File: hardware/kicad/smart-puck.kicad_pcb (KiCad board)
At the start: 2 copper layers, 3 parts, among them U1 ESP32-C6-MINI-1, U2 TPS63900, U3 SHT4x

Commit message: worked on schematic
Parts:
- added J1: HLK-LD2420, Connector_PinHeader_2.54mm:PinHeader_1x04_P2.54mm_Vertical, F.Cu at (125.8, 112.3)
- added U4: BQ25185DLHR, BQ25185:WSON10_DLH_TEX, F.Cu at (136.5, 113.0)
- added U5: MAX17048G+T10, MAX17048G:21-0168E_T822-3_MXM, F.Cu at (136.0, 118.2)

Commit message: worked on schematic
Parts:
- added J2: HLK-LD2420, Connector_PinSocket_2.54mm:PinSocket_1x05_P2.54mm_Vertical, F.Cu at (146.8, 141.8)
- added U2: TPS63900, Package_SON:WSON-10-1EP_2.5x2.5mm_P0.5mm_EP1.2x2mm_ThermalVias, F.Cu at (151.9, 141.5)
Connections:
- U1 pad 1: Net-(U1-GND-Pad1) -> BAT-
- U1 pad 11: Net-(U1-GND-Pad1) -> BAT-
- U1 pad 12: unconnected-(U1-IO0-Pad12) -> OT2
- U1 pad 14: Net-(U1-GND-Pad1) -> BAT-
- U1 pad 17: unconnected-(U1-IO12-Pad17) -> D-
- U1 pad 18: unconnected-(U1-IO13-Pad18) -> D+
- U1 pad 2: Net-(U1-GND-Pad1) -> BAT-
- U1 pad 22: unconnected-(U1-IO8-Pad22) -> BOOT
- U1 pad 24: unconnected-(U1-IO18-Pad24) -> RX
- U1 pad 25: unconnected-(U1-IO19-Pad25) -> TX
- U1 pad 27: unconnected-(U1-IO21-Pad27) -> LED_R
- U1 pad 28: unconnected-(U1-IO22-Pad28) -> LED_G
- U1 pad 29: unconnected-(U1-IO23-Pad29) -> LED_B
- U1 pad 3: unconnected-(U1-3V3-Pad3) -> +3.3V
- U1 pad 36: Net-(U1-GND-Pad1) -> BAT-
- U1 pad 37: Net-(U1-GND-Pad1) -> BAT-
- U1 pad 38: Net-(U1-GND-Pad1) -> BAT-
- U1 pad 39: Net-(U1-GND-Pad1) -> BAT-
- U1 pad 40: Net-(U1-GND-Pad1) -> BAT-
- U1 pad 41: Net-(U1-GND-Pad1) -> BAT-
- U1 pad 42: Net-(U1-GND-Pad1) -> BAT-
- U1 pad 43: Net-(U1-GND-Pad1) -> BAT-
- U1 pad 44: Net-(U1-GND-Pad1) -> BAT-
- U1 pad 45: Net-(U1-GND-Pad1) -> BAT-
- U1 pad 46: Net-(U1-GND-Pad1) -> BAT-
- U1 pad 47: Net-(U1-GND-Pad1) -> BAT-
- U1 pad 48: Net-(U1-GND-Pad1) -> BAT-
- U1 pad 49: Net-(U1-GND-Pad1) -> BAT-
- U1 pad 5: unconnected-(U1-IO2-Pad5) -> SDA
- U1 pad 50: Net-(U1-GND-Pad1) -> BAT-
- U1 pad 51: Net-(U1-GND-Pad1) -> BAT-
- U1 pad 52: Net-(U1-GND-Pad1) -> BAT-
- U1 pad 53: Net-(U1-GND-Pad1) -> BAT-
- U1 pad 6: unconnected-(U1-IO3-Pad6) -> SCL
- U1 pad 8: unconnected-(U1-EN-Pad8) -> EN
- U3 pad 1: unconnected-(U3-SDA-Pad1) -> SDA
- U3 pad 2: unconnected-(U3-SCL-Pad2) -> SCL
- U3 pad 3: unconnected-(U3-VDD-Pad3) -> +3.3V
- U3 pad 4: unconnected-(U3-VSS-Pad4) -> BAT-
- U4 pad 1: unconnected-(U4-SYS-Pad1) -> Net-(U4-SYS)
- U4 pad 10: unconnected-(U4-IN-Pad10) -> +5V
- U4 pad 11: unconnected-(U4-EPAD-Pad11) -> BAT-
- U4 pad 2: unconnected-(U4-BAT-Pad2) -> BAT+
- U4 pad 4: unconnected-(U4-/CE-Pad4) -> BAT-
- U4 pad 5: unconnected-(U4-GND-Pad5) -> BAT-
- U4 pad 6: unconnected-(U4-TS/MR-Pad6) -> Net-(U4-TS/MR)
- U4 pad 7: unconnected-(U4-ILIM/VSET-Pad7) -> Net-(U4-ILIM/VSET)
- U4 pad 8: unconnected-(U4-ISET-Pad8) -> Net-(U4-ISET)
- U5 pad 1: unconnected-(U5-CTG-Pad1) -> BAT-
- U5 pad 3: unconnected-(U5-VDD-Pad3) -> BAT+
- U5 pad 4: unconnected-(U5-GND-Pad4) -> BAT-
- U5 pad 6: unconnected-(U5-QSTRT-Pad6) -> BAT-
- U5 pad 7: unconnected-(U5-SCL-Pad7) -> SCL
- U5 pad 8: unconnected-(U5-SDA-Pad8) -> SDA
- U5 pad 9: unconnected-(U5-EPAD-Pad9) -> BAT-

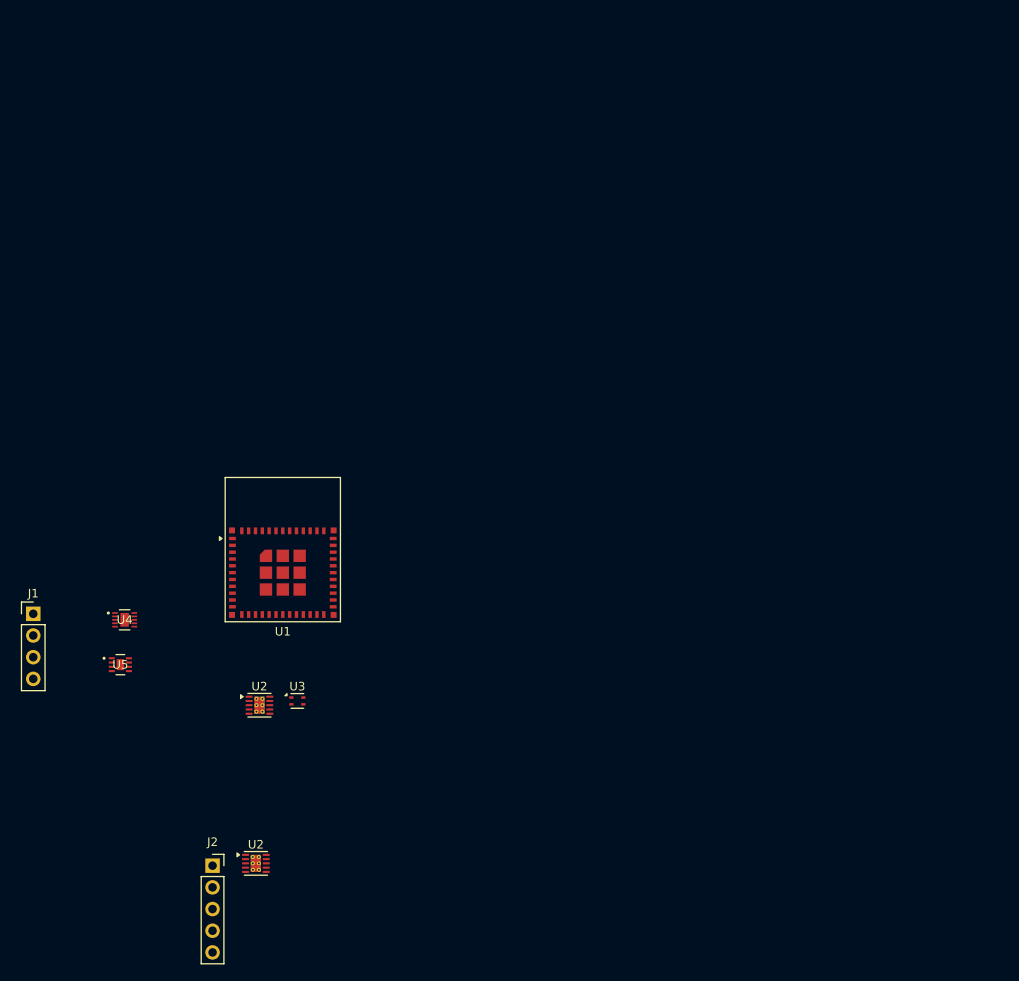
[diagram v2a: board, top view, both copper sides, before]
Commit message: add footprints and start working on pcb layout
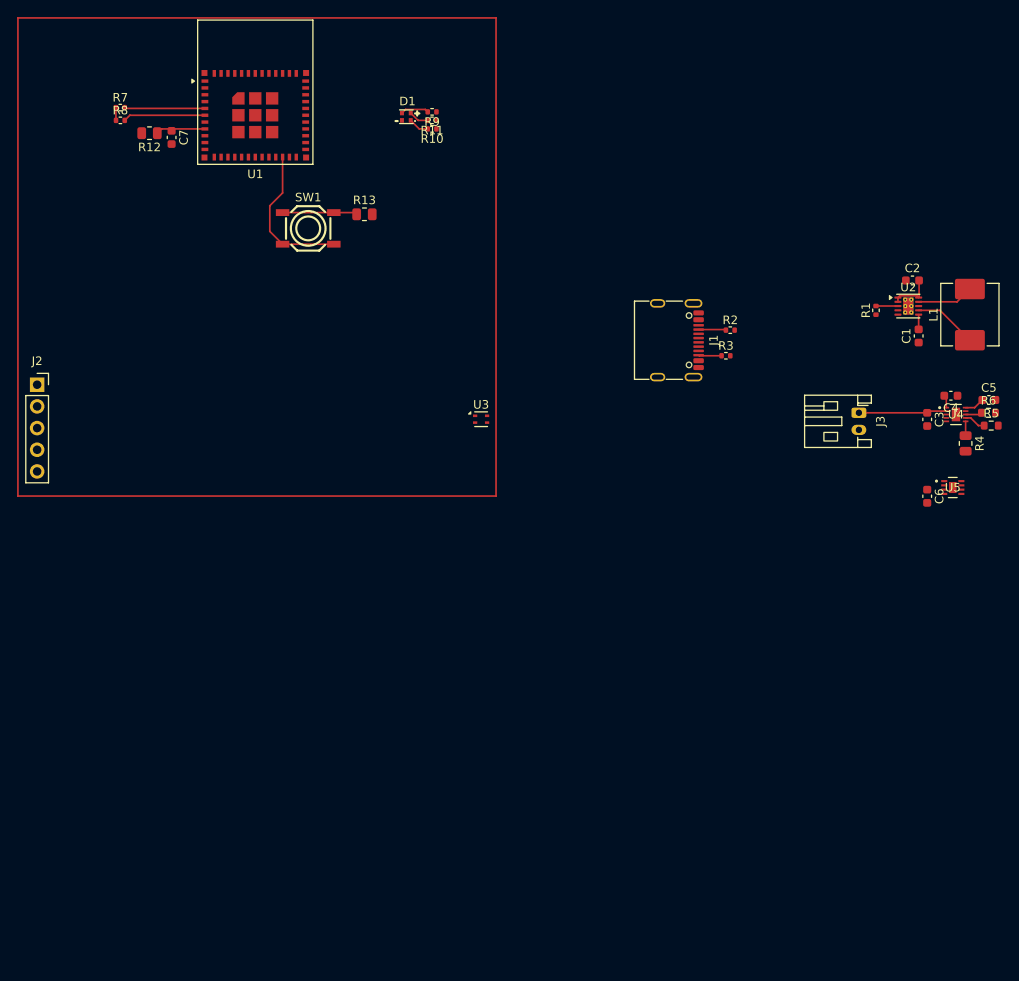
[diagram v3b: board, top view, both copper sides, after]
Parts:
- removed the U2 at (152.3, 123.0)
- removed the U2 at (151.9, 141.5)
- added C1: 22uF, Capacitor_SMD:C_0603_1608Metric, F.Cu at (229.5, 79.8)
- added C2: 10uF, Capacitor_SMD:C_0603_1608Metric, F.Cu at (228.8, 73.2)
- added C3: 1uF, Capacitor_SMD:C_0603_1608Metric, F.Cu at (230.5, 89.5)
- added C4: 10uF, Capacitor_SMD:C_0603_1608Metric, F.Cu at (233.3, 86.8)
- added C5: 1uF, Capacitor_SMD:C_0603_1608Metric, F.Cu at (237.7, 87.2)
- added C6: 0.1uF, Capacitor_SMD:C_0603_1608Metric, F.Cu at (230.5, 98.5)
- added C7: 1uF, Capacitor_SMD:C_0603_1608Metric, F.Cu at (142.0, 56.5)
- added D1: RS-C1415MBAR, RS-C1415MBAR:LED-ARRAY-SMD_4P-L1.6-W1.6-BR-RD-CW, F.Cu at (169.5, 54.1)
- added J3: Battery, Connector_JST:JST_PH_S2B-PH-K_1x02_P2.00mm_Horizontal, F.Cu at (222.5, 88.8)
- added L1: 2.2uH 30mOhm, Inductor_SMD:L_TechFuse_SL0624, F.Cu at (235.5, 77.2)
- added R1: 36.5kOhm, Resistor_SMD:R_0402_1005Metric, F.Cu at (224.5, 76.8)
- added R10: 68Ohm, Resistor_SMD:R_0402_1005Metric, F.Cu at (172.5, 55.5)
- added R11: 100Ohm, Resistor_SMD:R_0402_1005Metric, F.Cu at (172.5, 54.5)
- added R12: 10kOhm, Resistor_SMD:R_0805_2012Metric, F.Cu at (139.4, 56.0)
- added R13: 10kOhm, Resistor_SMD:R_0805_2012Metric, F.Cu at (164.6, 65.5)
- added R2: 5.1kOhm, Resistor_SMD:R_0402_1005Metric, F.Cu at (207.4, 79.1)
- added R3: 5.1kOhm, Resistor_SMD:R_0402_1005Metric, F.Cu at (206.9, 82.1)
- added R4: 10kOhm, Resistor_SMD:R_0805_2012Metric, F.Cu at (235.0, 92.3)
- added R5: 18kOhm, Resistor_SMD:R_0603_1608Metric, F.Cu at (238.0, 90.2)
- added R6: 1kOhm, Resistor_SMD:R_0603_1608Metric, F.Cu at (237.7, 88.8)
- added R7: 4.7kOhm, Resistor_SMD:R_0402_1005Metric, F.Cu at (136.0, 53.0)
- added R8: 4.7kOhm, Resistor_SMD:R_0402_1005Metric, F.Cu at (136.0, 54.5)
- added R9: 68Ohm, Resistor_SMD:R_0402_1005Metric, F.Cu at (172.5, 53.5)
- added SW1: GT-TZ084B-H015-L1, GT-TZ084B-H015-L1:SW-SMD_4P-L5.2-W5.2-P3.70-LS6.4, F.Cu at (158.0, 67.2)
- added U2: TPS63900, Package_SON:WSON-10-1EP_2.5x2.5mm_P0.5mm_EP1.2x2mm_ThermalVias, F.Cu at (228.3, 76.2)
- J1: value HLK-LD2420 -> USB_C_Receptacle_USB2.0_16P; footprint Connector_PinHeader_2.54mm:PinHeader_1x04_P2.54mm_Vertical -> Connector_USB:USB_C_Receptacle_G-Switch_GT-USB-7010ASV
- moved U4 100.3 mm to (233.9, 88.9)
- moved U5 99.7 mm to (233.5, 97.5)
- moved J1 80.8 mm to (200.0, 80.2), turned to -90 degrees
- moved J2 60.0 mm to (126.2, 85.5)
- moved U1 53.7 mm to (151.8, 53.9)
- moved U3 39.4 mm to (178.2, 89.5)
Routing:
- net BOOT: track 0.00 -> 17.4 mm
- net BAT+: track 0.00 -> 15.4 mm
- net SCL: track 0.00 -> 9.64 mm
- net SDA: track 0.00 -> 9.44 mm
- net Net-(R13-Pad1): track 0.00 -> 8.76 mm
- net Net-(U2-LX2): track 0.00 -> 7.45 mm
- net Net-(U2-LX1): track 0.00 -> 6.62 mm
- net EN: track 0.00 -> 5.78 mm
- net Net-(D1-BA): track 0.00 -> 3.31 mm
- net +3.3V: track 0.00 -> 3.23 mm
- net Net-(J1-CC1): track 0.00 -> 3.23 mm
- net Net-(J1-CC2): track 0.00 -> 2.72 mm
- net Net-(U2-CFG1): track 0.00 -> 2.58 mm
- net Net-(U4-ILIM/VSET): track 0.00 -> 2.55 mm
- net Net-(D1-GA): track 0.00 -> 2.40 mm
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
